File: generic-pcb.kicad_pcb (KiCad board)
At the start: 2 copper layers, 99.1 x 99.1 mm, 249 parts

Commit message: tweak solder mask clearance
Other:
- rule pad_to_mask_clearance: 0.2 -> 0
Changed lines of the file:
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@@
     (uvia_drill 0.1)
     (uvias_allowed no)
-    (uvia_min_size 0.2)
-    (uvia_min_drill 0.1)
+    (uvia_min_size 0)
+    (uvia_min_drill 0)
     (pcb_text_width 0.3)
     (pcb_text_size 1.5 1.5)
@@
     (pad_size 1.524 1.524)
     (pad_drill 0.762)
-    (pad_to_mask_clearance 0.2)
-    (aux_axis_origin 0 0)
+    (pad_to_mask_clearance 0)
+    (aux_axis_origin 97.79 43.18)
+    (grid_origin 97.79 43.18)
     (visible_elements FFFFFF7F)
     (pcbplotparams
-      (layerselection 0x01030_80000001)
+      (layerselection 0x010f0_80000001)
       (usegerberextensions true)
       (excludeedgelayer true)

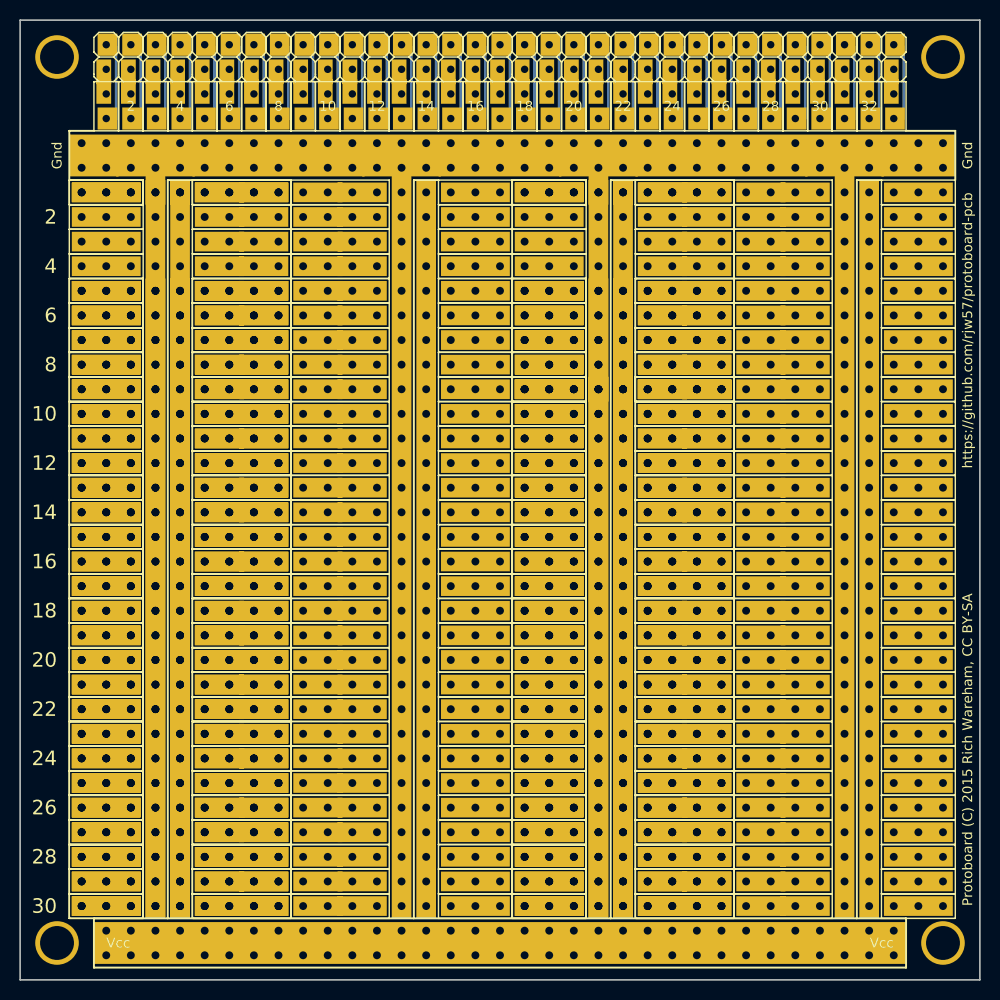
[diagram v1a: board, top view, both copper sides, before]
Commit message: make top header boxed IDC friendly
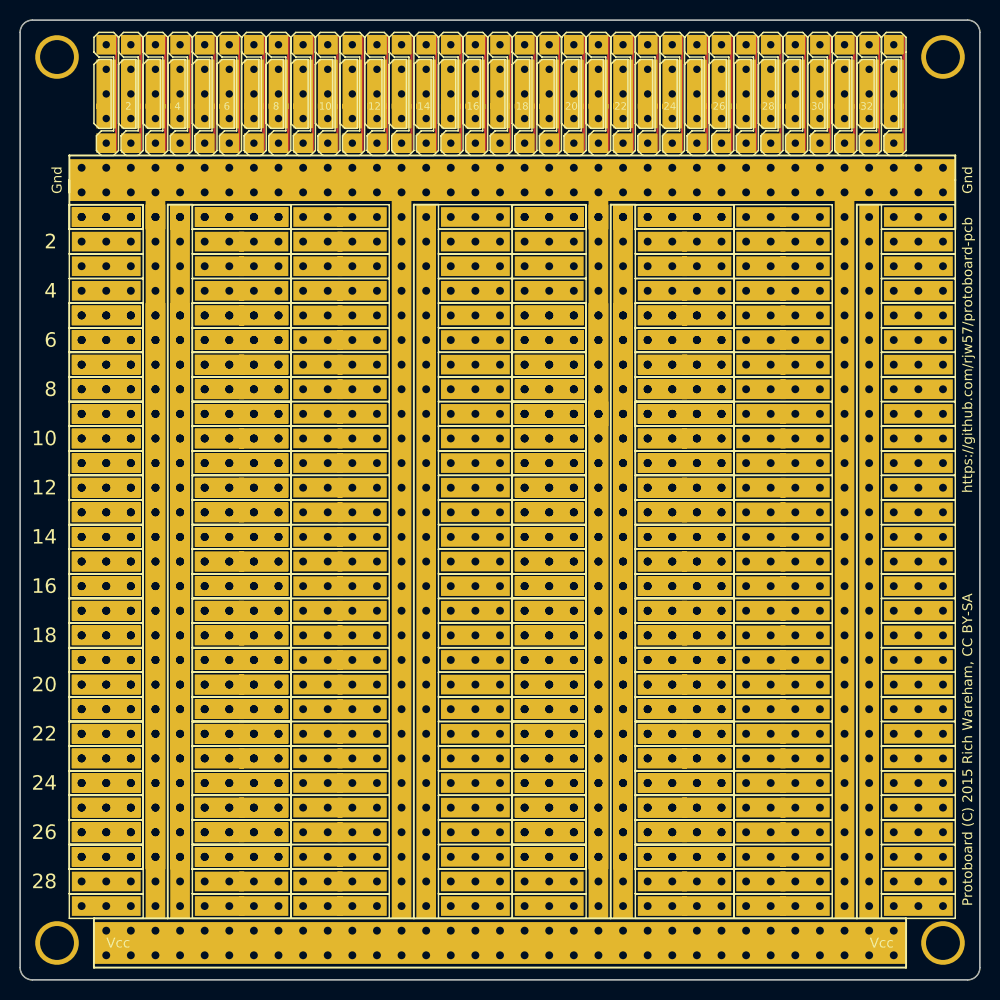
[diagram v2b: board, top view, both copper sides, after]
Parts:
- removed the REF**1 at (113.0, 134.6) (x2)
- removed the REF**1 at (158.8, 134.6) (x2)
- removed the REF**2 at (113.0, 132.1) (x2)
- removed the REF**2 at (158.8, 132.1) (x2)
- removed the REF**8 at (138.4, 134.6)
- removed the REF**8 at (184.2, 134.6)
- removed the REF**9 at (138.4, 132.1)
- removed the REF**9 at (184.2, 132.1)
- added REF**10: DIP pads, generic-pcb:DIP-pads, F.Cu at (184.2, 134.6)
- added REF**10: DIP pads, generic-pcb:DIP-pads, F.Cu at (138.4, 134.6)
- moved REF**3 5.08 mm to (113.0, 134.6)
- moved REF**3 5.08 mm to (158.8, 134.6)
- moved REF**10 2.54 mm to (138.4, 132.1)
- moved REF**10 2.54 mm to (184.2, 132.1)
- moved REF**3 2.54 mm to (113.0, 132.1)
- moved REF**3 2.54 mm to (158.8, 132.1)
- moved REF**11 2.54 mm to (113.0, 111.8) (x2)
- moved REF**11 2.54 mm to (158.8, 111.8) (x2)
- moved REF**12 2.54 mm to (138.4, 127.0)
- moved REF**12 2.54 mm to (184.2, 127.0)
- moved REF**13 2.54 mm to (113.0, 106.7) (x2)
- moved REF**13 2.54 mm to (158.8, 106.7)
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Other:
- outline, holes or cut-outs redrawn
